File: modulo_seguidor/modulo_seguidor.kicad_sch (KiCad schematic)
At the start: 26 parts, among them J1 Battery, J6 puerto sensores, M1 Motor_IZQ, M2 Motor_DER, SW1 SW_Push, SW2 SW_Nidec_CAS-120A1, U1 LM7806_TO220, U2 L298N

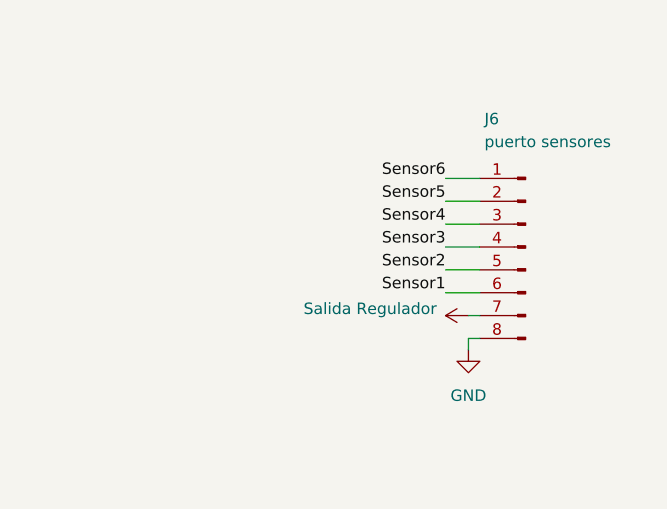
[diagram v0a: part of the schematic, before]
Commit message: refactor(seguidor): Reordeno los pines del modulo sensor
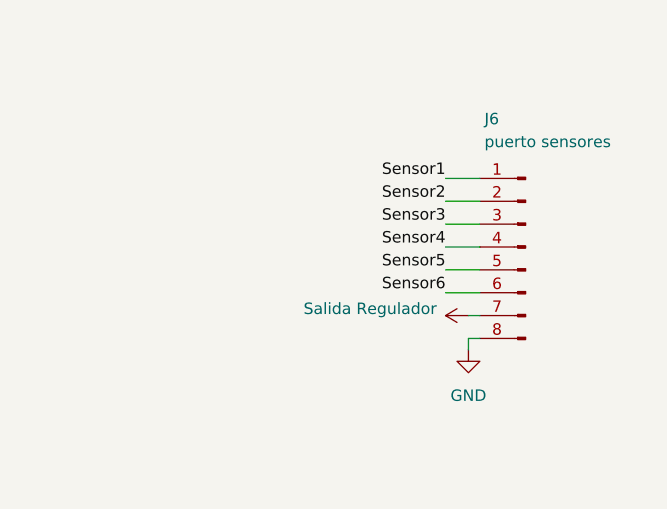
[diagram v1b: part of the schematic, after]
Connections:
- net Sensor1: now also J6.1 (Pin_1); no longer J6.6 (Pin_6)
- net Sensor2: now also J6.2 (Pin_2); no longer J6.5 (Pin_5)
- net Sensor3: now also J6.3 (Pin_3); no longer J6.4 (Pin_4)
- net Sensor4: now also J6.4 (Pin_4); no longer J6.3 (Pin_3)
- net Sensor5: now also J6.5 (Pin_5); no longer J6.2 (Pin_2)
- net Sensor6: now also J6.6 (Pin_6); no longer J6.1 (Pin_1)
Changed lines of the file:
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@@
 	)
 	(label "Sensor3"
-		(at 237.49 39.37 180)
+		(at 237.49 36.83 180)
 		(effects
 			(font
@@
 	)
 	(label "Sensor2"
-		(at 237.49 41.91 180)
+		(at 237.49 34.29 180)
 		(effects
 			(font
@@
 	)
 	(label "Sensor1"
-		(at 237.49 44.45 180)
+		(at 237.49 31.75 180)
 		(effects
 			(font
@@
 	)
 	(label "Sensor6"
-		(at 237.49 31.75 180)
+		(at 237.49 44.45 180)
 		(effects
 			(font
@@
 	)
 	(label "Sensor5"
-		(at 237.49 34.29 180)
+		(at 237.49 41.91 180)
 		(effects
 			(font
@@
 	)
 	(label "Sensor4"
-		(at 237.49 36.83 180)
+		(at 237.49 39.37 180)
 		(effects
 			(font

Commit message: refactor(modulo-seguidor): Cambio resistencia del LED de THT por SMD
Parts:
- R2: footprint Resistor_THT:R_Axial_DIN0411_L9.9mm_D3.6mm_P12.70mm_Horizontal -> Resistor_SMD:R_1206_3216Metric_Pad1.30x1.75mm_HandSolder
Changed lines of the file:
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@@
 			)
 		)
-		(property "Footprint" "Resistor_THT:R_Axial_DIN0411_L9.9mm_D3.6mm_P12.70mm_Horizontal"
+		(property "Footprint" "Resistor_SMD:R_1206_3216Metric_Pad1.30x1.75mm_HandSolder"
 			(at 182.626 67.564 90)
 			(effects

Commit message: refactor(modulo-seguidor): Cambio huella de motores a Housing
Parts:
- M1, M2: footprint Resistor_THT:R_Axial_DIN0207_L6.3mm_D2.5mm_P2.54mm_Vertical -> Connector_Molex:Molex_KK-254_AE-6410-02A_1x02_P2.54mm_Vertical
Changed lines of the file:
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@@
 			)
 		)
-		(property "Footprint" "Resistor_THT:R_Axial_DIN0207_L6.3mm_D2.5mm_P2.54mm_Vertical"
+		(property "Footprint" "Connector_Molex:Molex_KK-254_AE-6410-02A_1x02_P2.54mm_Vertical"
 			(at 125.73 130.556 0)
 			(effects
@@
 			)
 		)
-		(property "Footprint" "Resistor_THT:R_Axial_DIN0207_L6.3mm_D2.5mm_P2.54mm_Vertical"
+		(property "Footprint" "Connector_Molex:Molex_KK-254_AE-6410-02A_1x02_P2.54mm_Vertical"
 			(at 125.73 164.846 0)
 			(effects

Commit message: Update modulo_seguidor.kicad_sch
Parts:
- C1, C2, C3, C4: footprint Capacitor_THT:C_Disc_D7.0mm_W2.5mm_P5.00mm -> Capacitor_SMD:C_1206_3216Metric_Pad1.33x1.80mm_HandSolder
- R1: footprint Resistor_THT:R_Axial_DIN0411_L9.9mm_D3.6mm_P12.70mm_Horizontal -> Resistor_SMD:R_1206_3216Metric_Pad1.30x1.75mm_HandSolder
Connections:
- net Boton_encendido: now also A1.16 (D13); no longer A1.11 (D8)
- net Entrada DIG Motor B: now also A1.11 (D8); no longer A1.14 (D11)
- net Entrada PWM Motor A: now also A1.14 (D11); no longer A1.12 (D9)
- net Entrada PWM Motor B: now also A1.12 (D9); no longer A1.15 (D12)
- net at D1.2 (A): now also A1.20 (A1); no longer A1.26 (A7)
- no-connect marks 16 -> 17
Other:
- moved on the sheet: D1, R2
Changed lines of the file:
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@@
 	)
 	(no_connect
-		(at 167.64 48.26)
+		(at 167.64 63.5)
 	)
 	(no_connect
@@
 	)
 	(no_connect
+		(at 48.26 82.55)
+	)
+	(no_connect
 		(at 167.64 30.48)
 	)
 	(no_connect
+		(at 142.24 60.96)
+	)
+	(no_connect
 		(at 167.64 53.34)
 	)
@@
 	)
 	(no_connect
-		(at 142.24 63.5)
-	)
-	(no_connect
 		(at 167.64 50.8)
 	)
@@
 	(wire
 		(pts
+			(xy 167.64 48.26) (xy 171.45 48.26)
+		)
+		(stroke
+			(width 0)
+			(type default)
+		)
+	)
+	(wire
+		(pts
 			(xy 41.91 36.83) (xy 36.83 36.83)
 		)
@@
 	(wire
 		(pts
+			(xy 139.7 53.34) (xy 142.24 53.34)
+		)
+		(stroke
+			(width 0)
+			(type default)
+		)
+	)
+	(wire
+		(pts
 			(xy 125.73 157.48) (xy 125.73 154.94)
 		)
@@
 	(wire
 		(pts
-			(xy 139.7 50.8) (xy 142.24 50.8)
+			(xy 80.01 167.64) (xy 80.01 166.37)
 		)
 		(stroke
@@
 	(wire
 		(pts
-			(xy 80.01 167.64) (xy 80.01 166.37)
+			(xy 63.5 167.64) (xy 72.39 167.64)
 		)
 		(stroke
@@
 	(wire
 		(pts
-			(xy 63.5 167.64) (xy 72.39 167.64)
+			(xy 139.7 50.8) (xy 142.24 50.8)
 		)
 		(stroke
@@
 	(wire
 		(pts
-			(xy 113.03 120.65) (xy 114.3 120.65)
+			(xy 138.43 63.5) (xy 142.24 63.5)
 		)
 		(stroke
@@
 	(wire
 		(pts
-			(xy 63.5 167.64) (xy 57.15 167.64)
+			(xy 113.03 120.65) (xy 114.3 120.65)
 		)
 		(stroke
@@
 	(wire
 		(pts
-			(xy 168.91 63.5) (xy 167.64 63.5)
+			(xy 63.5 167.64) (xy 57.15 167.64)
 		)
 		(stroke
@@
 	(wire
 		(pts
-			(xy 181.61 71.12) (xy 181.61 72.39)
+			(xy 184.15 55.88) (xy 184.15 57.15)
 		)
 		(stroke
@@
 	(wire
 		(pts
-			(xy 142.24 60.96) (xy 139.7 60.96)
+			(xy 139.7 55.88) (xy 142.24 55.88)
 		)
 		(stroke
@@
 	(wire
 		(pts
-			(xy 176.53 63.5) (xy 181.61 63.5)
-		)
-		(stroke
-			(width 0)
-			(type default)
-		)
-	)
-	(wire
-		(pts
-			(xy 142.24 58.42) (xy 139.7 58.42)
+			(xy 179.07 48.26) (xy 184.15 48.26)
 		)
 		(stroke
@@
 	(wire
 		(pts
-			(xy 139.7 53.34) (xy 142.24 53.34)
-		)
-		(stroke
-			(width 0)
-			(type default)
-		)
-	)
-	(wire
-		(pts
 			(xy 74.93 179.07) (xy 74.93 177.8)
 		)
@@
 	(wire
 		(pts
-			(xy 102.87 180.34) (xy 125.73 180.34)
+			(xy 139.7 58.42) (xy 142.24 58.42)
 		)
 		(stroke
@@
 	(wire
 		(pts
-			(xy 125.73 135.89) (xy 125.73 139.7)
+			(xy 102.87 180.34) (xy 125.73 180.34)
 		)
 		(stroke
@@
 	(wire
 		(pts
-			(xy 87.63 73.66) (xy 87.63 74.93)
+			(xy 125.73 135.89) (xy 125.73 139.7)
 		)
 		(stroke
@@
 	(wire
 		(pts
-			(xy 125.73 120.65) (xy 125.73 116.84)
+			(xy 87.63 73.66) (xy 87.63 74.93)
 		)
 		(stroke
@@
 	(wire
 		(pts
-			(xy 139.7 55.88) (xy 142.24 55.88)
+			(xy 125.73 120.65) (xy 125.73 116.84)
 		)
 		(stroke
@@
 	)
 	(label "Entrada PWM Motor B"
-		(at 139.7 60.96 180)
+		(at 139.7 53.34 180)
 		(effects
 			(font
@@
 	)
 	(label "Boton_encendido"
-		(at 139.7 50.8 180)
+		(at 138.43 63.5 180)
 		(effects
 			(font
@@
 	)
 	(label "Entrada PWM Motor A"
-		(at 139.7 53.34 180)
+		(at 139.7 58.42 180)
 		(effects
 			(font
@@
 	)
 	(label "Entrada DIG Motor B"
-		(at 139.7 58.42 180)
+		(at 139.7 50.8 180)
 		(effects
 			(font
@@
 			)
 		)
-		(property "Footprint" "Capacitor_THT:C_Disc_D7.0mm_W2.5mm_P5.00mm"
+		(property "Footprint" "Capacitor_SMD:C_1206_3216Metric_Pad1.33x1.80mm_HandSolder"
 			(at 74.93 121.92 0)
 			(effects
@@
 			)
 		)
-		(property "Footprint" "Capacitor_THT:C_Disc_D7.0mm_W2.5mm_P5.00mm"
+		(property "Footprint" "Capacitor_SMD:C_1206_3216Metric_Pad1.33x1.80mm_HandSolder"
 			(at 87.63 121.92 0)
 			(effects
@@
 			)
 		)
-		(property "Footprint" "Capacitor_THT:C_Disc_D7.0mm_W2.5mm_P5.00mm"
+		(property "Footprint" "Capacitor_SMD:C_1206_3216Metric_Pad1.33x1.80mm_HandSolder"
 			(at 51.7652 74.93 0)
 			(effects
@@
 	(symbol
 		(lib_id "Device:LED")
-		(at 172.72 63.5 180)
+		(at 175.26 48.26 180)
 		(unit 1)
 		(exclude_from_sim no)
@@
 		(dnp no)
 		(property "Reference" "D1"
-			(at 173.228 68.834 0)
+			(at 175.768 53.594 0)
 			(effects
 				(font
@@
 		)
 		(property "Value" "LED"
-			(at 173.228 66.294 0)
+			(at 175.768 51.054 0)
 			(effects
 				(font
@@
 		)
 		(property "Footprint" "LED_THT:LED_D5.0mm"
-			(at 172.72 63.5 0)
+			(at 175.26 48.26 0)
 			(effects
 				(font
@@
 		)
 		(property "Datasheet" "~"
-			(at 172.72 63.5 0)
+			(at 175.26 48.26 0)
 			(effects
 				(font
@@
 		)
 		(property "Description" "Light emitting diode"
-			(at 172.72 63.5 0)
+			(at 175.26 48.26 0)
 			(effects
 				(font
@@
 		)
 		(property "Sim.Pins" "1=K 2=A"
-			(at 172.72 63.5 0)
+			(at 175.26 48.26 0)
 			(effects
 				(font
@@
 	(symbol
 		(lib_id "Device:R_US")
-		(at 181.61 67.31 0)
+		(at 184.15 52.07 0)
 		(unit 1)
 		(exclude_from_sim no)
@@
 		(fields_autoplaced yes)
 		(property "Reference" "R2"
-			(at 184.15 66.0399 0)
+			(at 186.69 50.7999 0)
 			(effects
 				(font
@@
 		)
 		(property "Value" "330"
-			(at 184.15 68.5799 0)
+			(at 186.69 53.3399 0)
 			(effects
 				(font
@@
 		)
 		(property "Footprint" "Resistor_SMD:R_1206_3216Metric_Pad1.30x1.75mm_HandSolder"
-			(at 182.626 67.564 90)
+			(at 185.166 52.324 90)
 			(effects
 				(font
@@
 		)
 		(property "Datasheet" "~"
-			(at 181.61 67.31 0)
+			(at 184.15 52.07 0)
 			(effects
 				(font
@@
 		)
 		(property "Description" "Resistor, US symbol"
-			(at 181.61 67.31 0)
+			(at 184.15 52.07 0)
 			(effects
 				(font
@@
 	(symbol
 		(lib_id "power:GND")
-		(at 181.61 72.39 0)
+		(at 184.15 57.15 0)
 		(unit 1)
 		(exclude_from_sim no)
@@
 		(fields_autoplaced yes)
 		(property "Reference" "#PWR06"
-			(at 181.61 78.74 0)
+			(at 184.15 63.5 0)
 			(effects
 				(font
@@
 		)
 		(property "Value" "GND"
-			(at 181.61 77.47 0)
+			(at 184.15 62.23 0)
 			(effects
 				(font
@@
 		)
 		(property "Footprint" ""
-			(at 181.61 72.39 0)
+			(at 184.15 57.15 0)
 			(effects
 				(font
@@
 		)
 		(property "Datasheet" ""
-			(at 181.61 72.39 0)
+			(at 184.15 57.15 0)
 			(effects
 				(font
@@
 		)
 		(property "Description" "Power symbol creates a global label with name \"GND\" , ground"
-			(at 181.61 72.39 0)
+			(at 184.15 57.15 0)
 			(effects
 				(font
@@
 			)
 		)
-		(property "Footprint" "Resistor_THT:R_Axial_DIN0411_L9.9mm_D3.6mm_P12.70mm_Horizontal"
+		(property "Footprint" "Resistor_SMD:R_1206_3216Metric_Pad1.30x1.75mm_HandSolder"
 			(at 88.646 78.994 90)
 			(effects
@@
 			)
 		)
-		(property "Footprint" "Capacitor_THT:C_Disc_D7.0mm_W2.5mm_P5.00mm"
+		(property "Footprint" "Capacitor_SMD:C_1206_3216Metric_Pad1.33x1.80mm_HandSolder"
 			(at 73.3552 41.91 0)
 			(effects

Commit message: Cambio de pines de motores
El anterior los había  cambiado para probar pero como mi idea ahora es usar housing para conectar con cable por arriba vuelvo a poner las entradas del motor en orden
PWM A = D ocho
 DIG  A  = D9
PWM B = D10
DIG B   = D11
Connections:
- net Entrada DIG Motor A: now also A1.12 (D9); no longer A1.13 (D10)
- net Entrada DIG Motor B: now also A1.14 (D11); no longer A1.11 (D8)
- net Entrada PWM Motor A: now also A1.11 (D8); no longer A1.14 (D11)
- net Entrada PWM Motor B: now also A1.13 (D10); no longer A1.12 (D9)

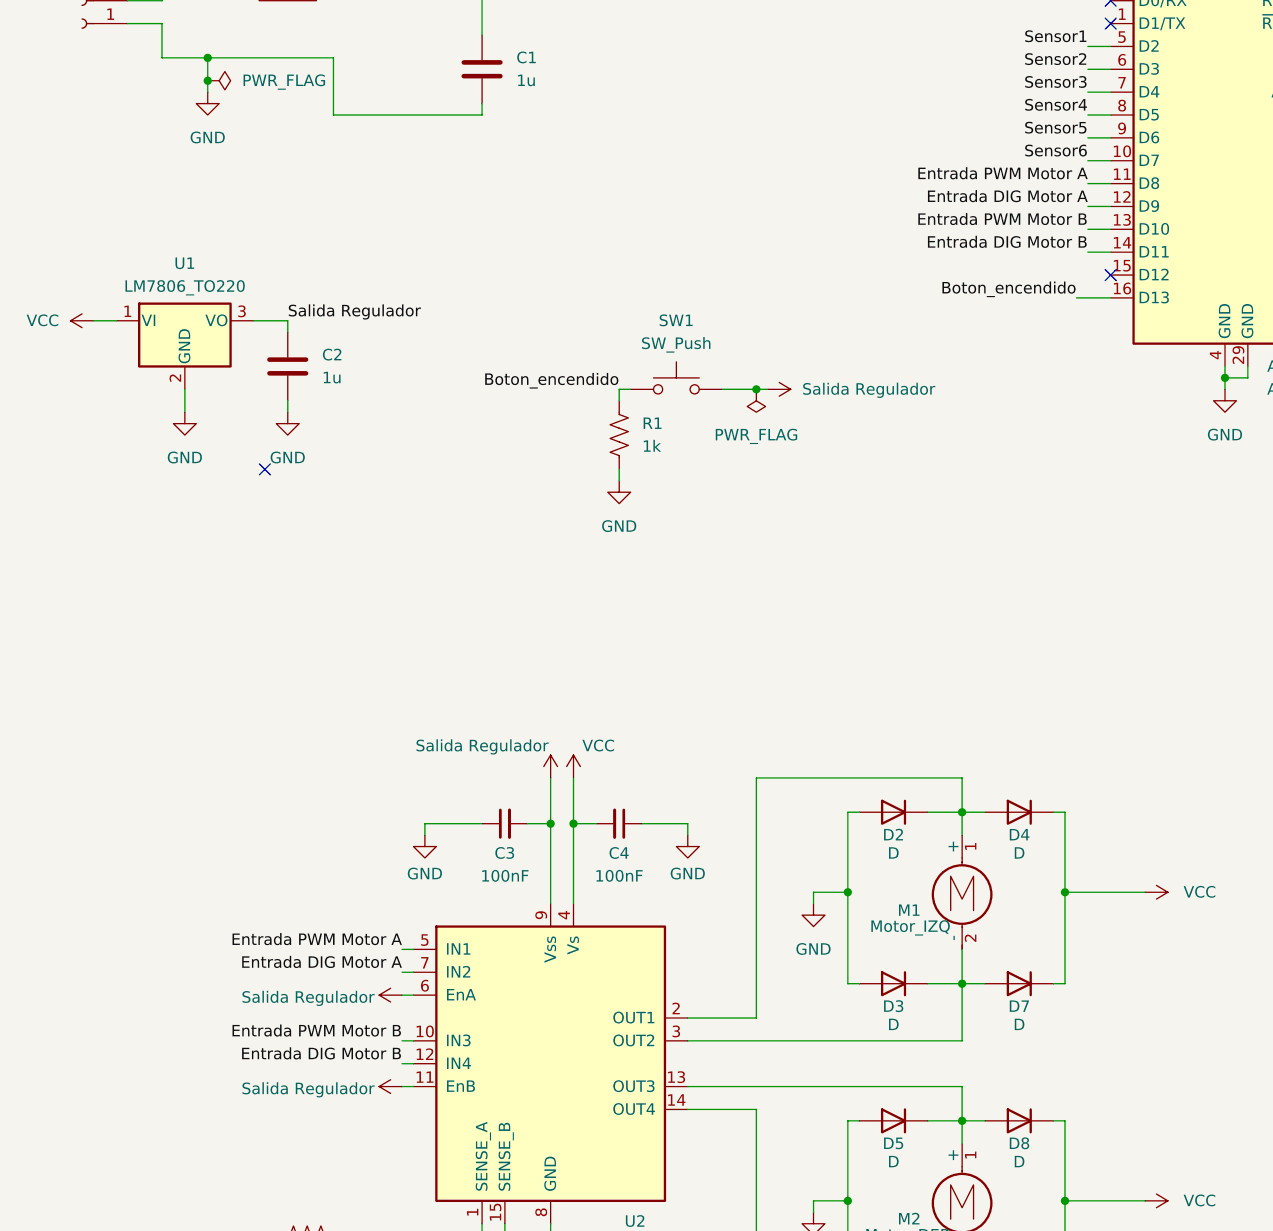
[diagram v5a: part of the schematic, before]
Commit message: refactor(modulo-seguidor): Cambio conexiones de entrada del l298 por housings
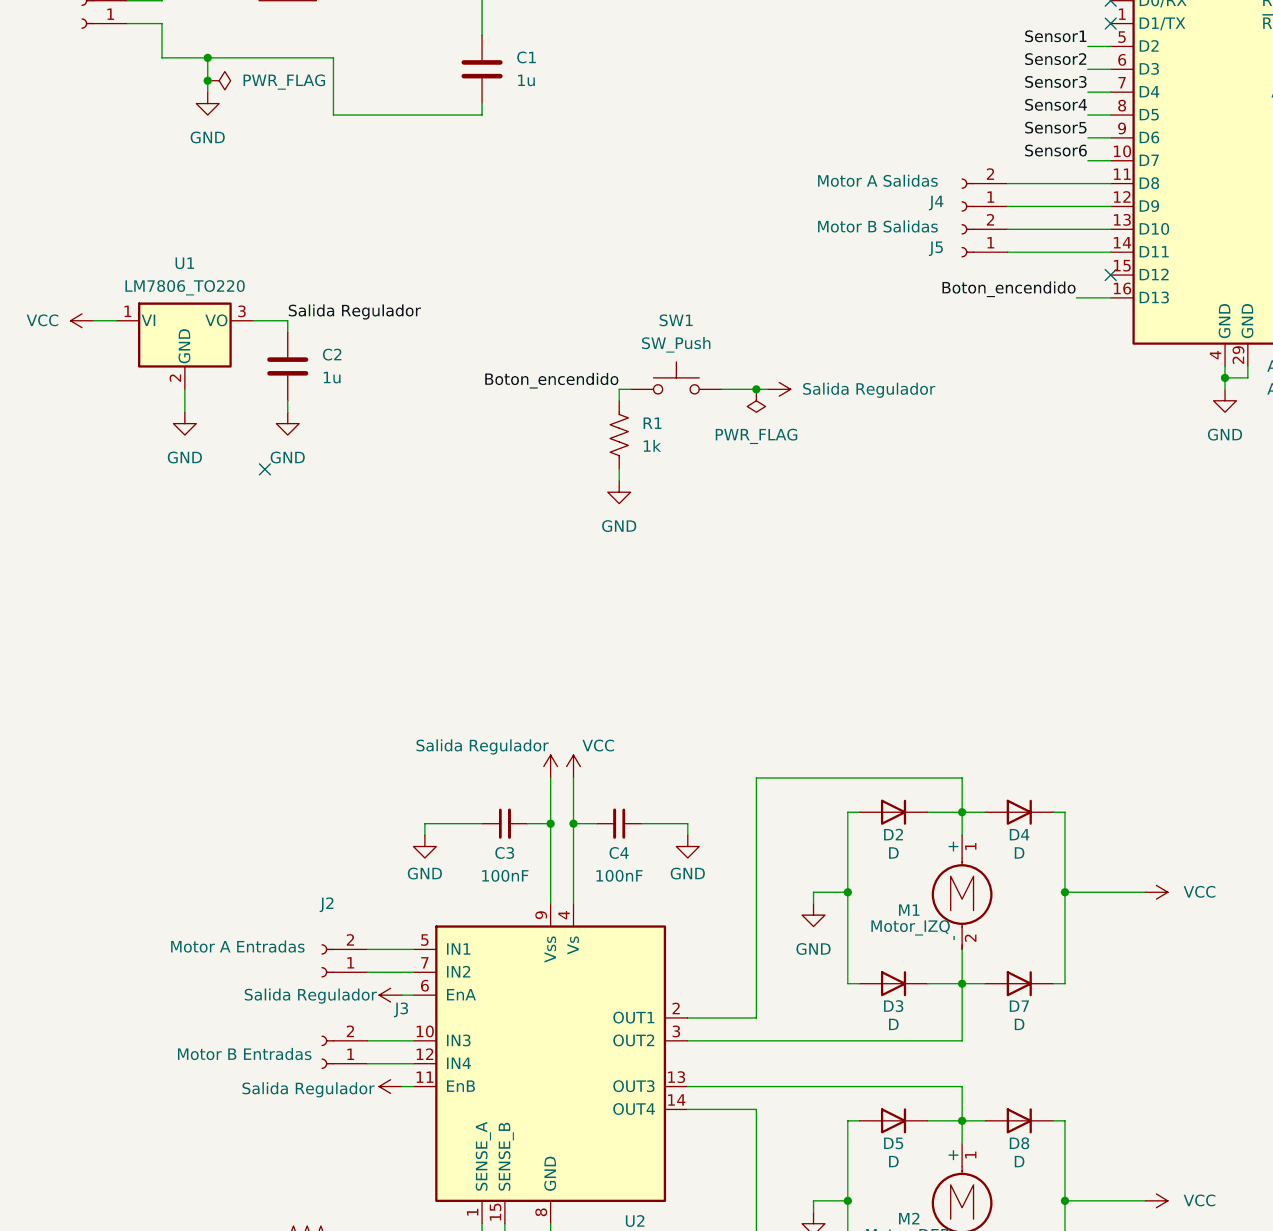
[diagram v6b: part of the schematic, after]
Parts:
- added J2: Motor A Entradas, Connector_Molex:Molex_KK-254_AE-6410-02A_1x02_P2.54mm_Vertical, symbol Connector:Conn_01x02_Socket
- added J3: Motor B Entradas, Connector_Molex:Molex_KK-254_AE-6410-02A_1x02_P2.54mm_Vertical, symbol Connector:Conn_01x02_Socket
- added J4: Motor A Salidas, Connector_Molex:Molex_KK-254_AE-6410-02A_1x02_P2.54mm_Vertical, symbol Connector:Conn_01x02_Socket
- added J5: Motor B Salidas, Connector_Molex:Molex_KK-254_AE-6410-02A_1x02_P2.54mm_Vertical, symbol Connector:Conn_01x02_Socket
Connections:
- net Entrada DIG Motor A: no longer names the net of U2.7 (IN2)
- net Entrada DIG Motor A: now also J2.1 (Pin_1); no longer A1.12 (D9)
- net Entrada DIG Motor B: no longer names the net of A1.14 (D11)
- net Entrada DIG Motor B: now also J5.1 (Pin_1); no longer U2.12 (IN4)
- net Entrada PWM Motor A: no longer names the net of U2.5 (IN1)
- net Entrada PWM Motor A: now also J2.2 (Pin_2); no longer A1.11 (D8)
- net Entrada PWM Motor B: no longer names the net of A1.13 (D10)
- net Entrada PWM Motor B: now also J5.2 (Pin_2); no longer U2.10 (IN3)
- new net: A1.12 (D9), J4.1 (Pin_1)
- new net: A1.11 (D8), J4.2 (Pin_2)
- new net: J3.2 (Pin_2), U2.10 (IN3)
- new net: J3.1 (Pin_1), U2.12 (IN4)
